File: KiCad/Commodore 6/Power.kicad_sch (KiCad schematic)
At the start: 33 parts, among them J3 6130XX11121_61300511121, Q1 NTR4501NT1G, Q2 PMOS

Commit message: Added most footprints
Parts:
- BMS1: footprint (none) -> BQ29209DRBR Protection IC:DRB8_1P6X2P4
- BatteryConnector1: footprint (none) -> Connector_JST:JST_XA_B03B-XASK-1_1x03_P2.50mm_Vertical
- C19: footprint WCAP-ASLL_4X5.5:WCAP-ASLL_4X5.5_DXL_ -> 865060640001 1uf electrolytic:WCAP-ASLL_4X5.5_DXL_
- C25: footprint WCAP-ASLI_5X5.5:WCAP-ASLI_5X5.5_DXL_ -> 865080342006 47uf electrolytic:WCAP-ASLI_5X5.5_DXL_
- DSUB1: footprint ICD15S13E4GX00LF:AMPHENOL_ICD15S13E4GX00LF -> ICD15S13E4GX00LF dsub:AMPHENOL_ICD15S13E4GX00LF
- J3: footprint 6130XX11121_61300511121:61300511121 -> 61300511121 5pin header:61300511121
- Payload_Header1: footprint (none) -> Connector_JST:JST_XA_B02B-XASK-1_1x02_P2.50mm_Vertical
- R10, R3, R4, R5: footprint (none) -> Resistor_SMD:R_1206_3216Metric
- TP1: footprint RCWCTE:TP420X150 -> RCWCTE testpoint:TP420X150
- schottkey1: footprint PDS1040L-13:DIO_PDS1040L-13 -> PDS1040L_13 schottkey:DIO_PDS1040L-13
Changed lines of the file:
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@@
 			)
 		)
-		(property "Footprint" "6130XX11121_61300511121:61300511121"
+		(property "Footprint" "61300511121 5pin header:61300511121"
 			(at 175.26 27.94 0)
 			(effects
@@
 			)
 		)
-		(property "Footprint" ""
+		(property "Footprint" "Resistor_SMD:R_1206_3216Metric"
 			(at 99.06 46.99 0)
 			(effects
@@
 			)
 		)
-		(property "Footprint" ""
+		(property "Footprint" "Resistor_SMD:R_1206_3216Metric"
 			(at 40.64 52.07 0)
 			(effects
@@
 		(on_board yes)
 		(dnp no)
-		(fields_autoplaced yes)
 		(property "Reference" "schottkey1"
 			(at 151.13 133.35 0)
@@
 			)
 		)
-		(property "Footprint" "PDS1040L-13:DIO_PDS1040L-13"
-			(at 151.13 139.7 0)
+		(property "Footprint" "PDS1040L_13 schottkey:DIO_PDS1040L-13"
+			(at 151.13 130.302 0)
 			(effects
 				(font
@@
 			)
 		)
-		(property "Footprint" ""
+		(property "Footprint" "Resistor_SMD:R_1206_3216Metric"
 			(at 31.75 111.76 0)
 			(effects
@@
 			)
 		)
-		(property "Footprint" ""
+		(property "Footprint" "Connector_JST:JST_XA_B02B-XASK-1_1x02_P2.50mm_Vertical"
 			(at 101.6 31.75 0)
 			(effects
@@
 			)
 		)
-		(property "Footprint" ""
+		(property "Footprint" "Connector_JST:JST_XA_B03B-XASK-1_1x03_P2.50mm_Vertical"
 			(at 34.29 161.29 0)
 			(effects
@@
 			)
 		)
-		(property "Footprint" ""
+		(property "Footprint" "BQ29209DRBR Protection IC:DRB8_1P6X2P4"
 			(at 83.82 152.4 0)
 			(effects
@@
 			)
 		)
-		(property "Footprint" "WCAP-ASLL_4X5.5:WCAP-ASLL_4X5.5_DXL_"
+		(property "Footprint" "865060640001 1uf electrolytic:WCAP-ASLL_4X5.5_DXL_"
 			(at 44.45 24.13 0)
 			(effects
@@
 			)
 		)
-		(property "Footprint" "RCWCTE:TP420X150"
+		(property "Footprint" "RCWCTE testpoint:TP420X150"
 			(at 193.04 34.29 0)
 			(effects
@@
 			)
 		)
-		(property "Footprint" ""
+		(property "Footprint" "Resistor_SMD:R_1206_3216Metric"
 			(at 31.75 90.17 0)
 			(effects
@@
 			)
 		)
-		(property "Footprint" "ICD15S13E4GX00LF:AMPHENOL_ICD15S13E4GX00LF"
+		(property "Footprint" "ICD15S13E4GX00LF dsub:AMPHENOL_ICD15S13E4GX00LF"
 			(at 251.46 87.63 0)
 			(effects
@@
 			)
 		)
-		(property "Footprint" "WCAP-ASLI_5X5.5:WCAP-ASLI_5X5.5_DXL_"
+		(property "Footprint" "865080342006 47uf electrolytic:WCAP-ASLI_5X5.5_DXL_"
 			(at 92.71 39.37 0)
 			(effects

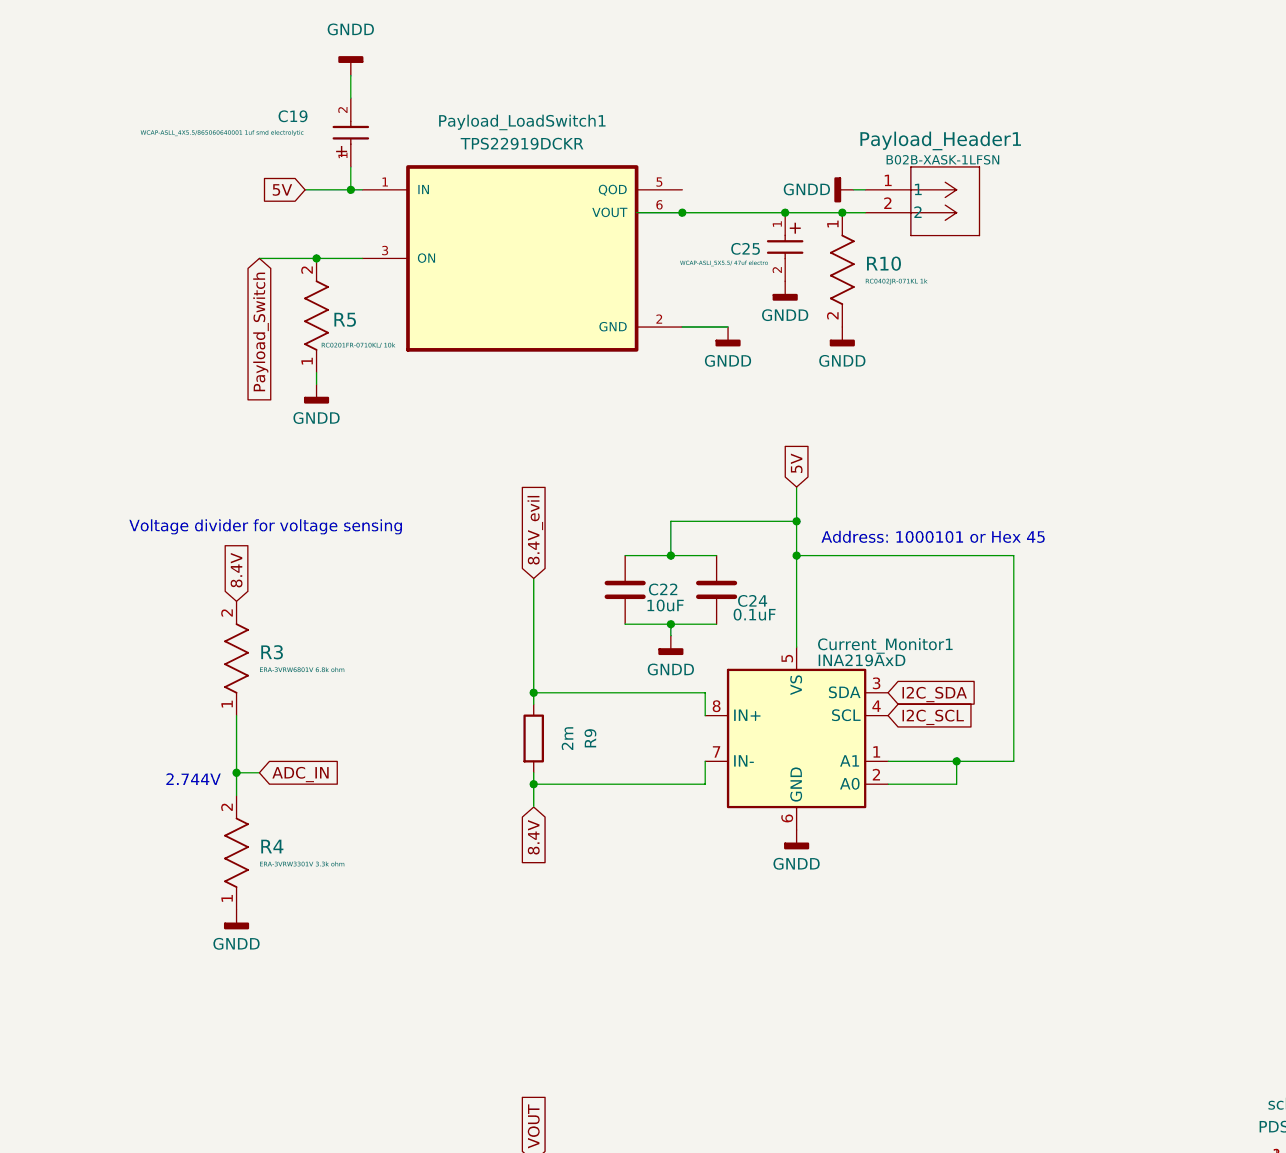
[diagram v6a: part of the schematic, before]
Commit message: Can start Routing
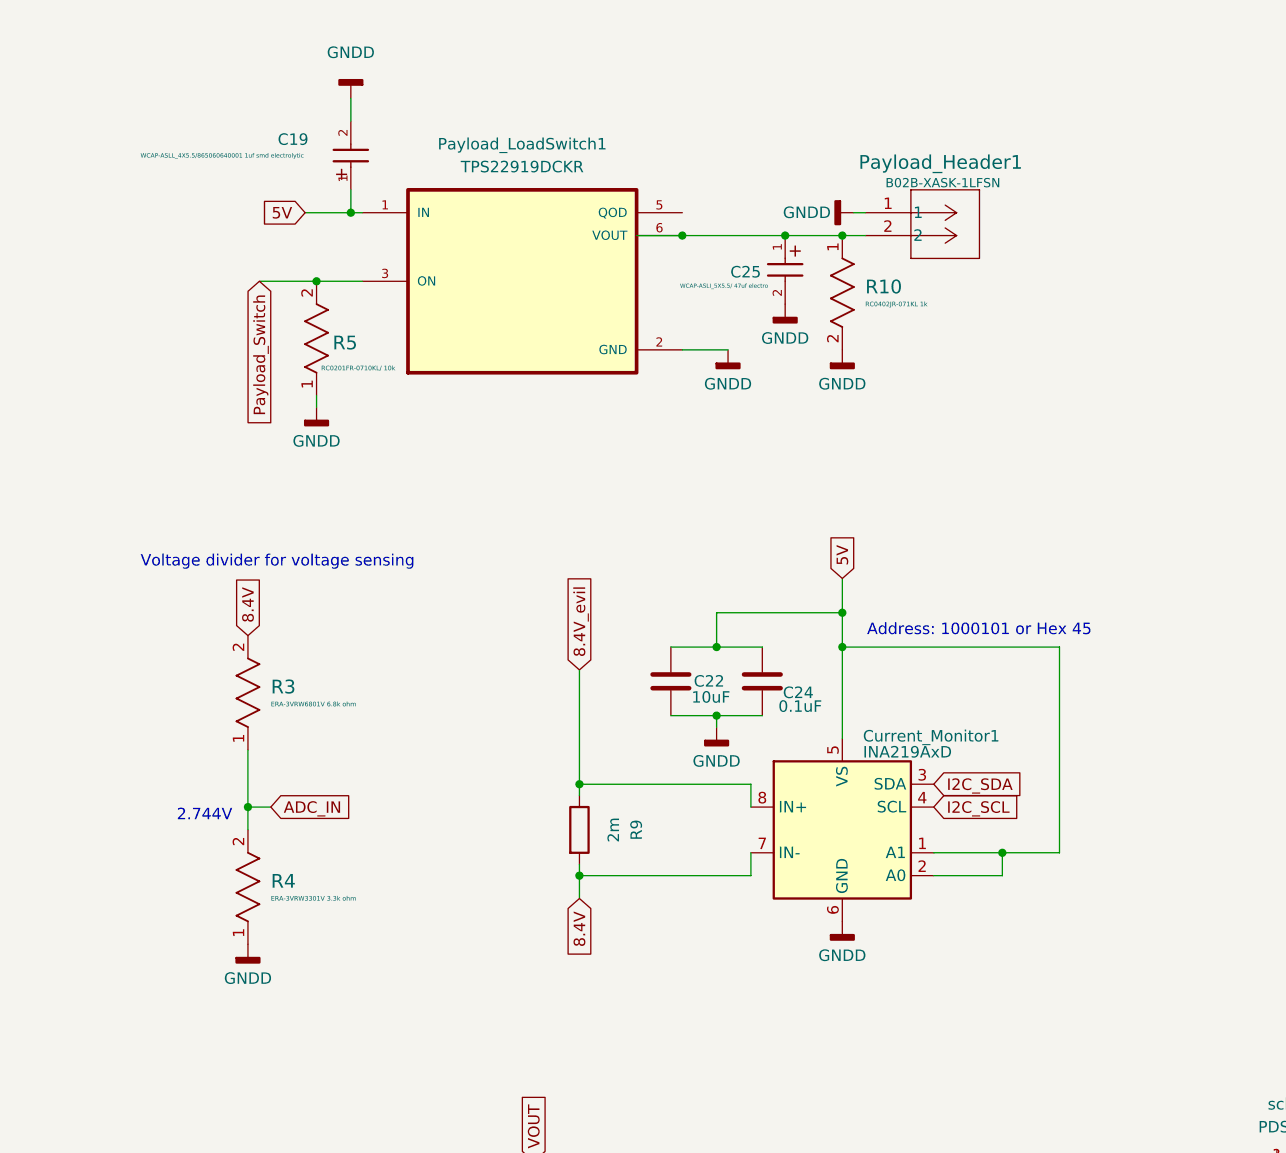
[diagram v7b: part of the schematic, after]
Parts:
- Q2: footprint (none) -> NTR4501NT1G:SOT95P237X111-3N
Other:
- moved on the sheet: C19, C22, C24, C25, Current_Monitor1, Payload_Header1, Payload_LoadSwitch1, R10, R3, R4, R5, R9

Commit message: bru
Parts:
- removed schottkey1: PDS1040L-13, PDS1040L_13 schottkey:DIO_PDS1040L-13, symbol PDS1040L-13:PDS1040L-13
- added J10: Conn_01x05_Pin, symbol Connector:Conn_01x05_Pin
- added Q3: 2N2219, Package_TO_SOT_THT:TO-39-3, symbol Transistor_BJT:2N2219
- added Q4: PMOS, NTR4501NT1G:SOT95P237X111-3N, symbol Simulation_SPICE:PMOS
- BatteryConnector1: footprint Connector_JST:JST_XA_B03B-XASK-1_1x03_P2.50mm_Vertical -> (none)
- C19: footprint 865060640001 1uf electrolytic:WCAP-ASLL_4X5.5_DXL_ -> WCAP-ASLL_4X5.5:WCAP-ASLL_4X5.5_DXL_
- C25: footprint 865080342006 47uf electrolytic:WCAP-ASLI_5X5.5_DXL_ -> WCAP-ASLI_5X5.5:WCAP-ASLI_5X5.5_DXL_
- DSUB1: footprint ICD15S13E4GX00LF dsub:AMPHENOL_ICD15S13E4GX00LF -> ICD15S13E4GX00LF:AMPHENOL_ICD15S13E4GX00LF
- J3: footprint 61300511121 5pin header:61300511121 -> 6130XX11121_61300511121:61300511121
- Payload_Header1: footprint Connector_JST:JST_XA_B02B-XASK-1_1x02_P2.50mm_Vertical -> (none)
- R10, R3, R4, R5: footprint Resistor_SMD:R_1206_3216Metric -> (none)
- TP1: footprint RCWCTE testpoint:TP420X150 -> RCWCTE:TP420X150
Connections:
- net GNDD: now also Q3.1 (E)
- net VOUT: now also C28.1, R12.2, R14.1, Q4.1 (D)
- net at C28.2, Q2.2 (G), R13.2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: now also Q4.2 (G)
- net at BMS1.8 (OUT): now also Q3.2 (B); no longer R12.1
- net at Q1.1: now also R12.1, Q3.3 (C); no longer R12.2
- new net: Q2.3 (S), Q4.3 (S)
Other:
- moved on the sheet: C27, C28, Q2, R12, R13, R14
